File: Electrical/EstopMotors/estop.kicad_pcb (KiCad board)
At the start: 2 copper layers, 20 parts, among them Q1 IRF530NPBF, Q2 IRF530NPBF, Q3 IRF530NPBF, Q4 IRF530NPBF

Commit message: updated to rev 2
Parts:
- removed 10k1, 10k2, 10k3, 10k4, 10k5, 10k6, 10k7, 10k8, 10k9: ROX5SSJ1K8, Resistor_THT:R_Axial_DIN0204_L3.6mm_D1.6mm_P7.62mm_Horizontal
- removed C1: ESK225M050AC3KA, Personal:CAPPRD200W50D500H1250
- removed Control: Conn_01x03, Connector_Wire:SolderWirePad_1x03_P7.62mm_Drill2.5mm
- removed Input 1-4: Conn_01x04, Connector_Wire:SolderWirePad_1x04_P7.62mm_Drill2.5mm
- removed Output 1-4: Conn_01x04, Connector_Wire:SolderWirePad_1x04_P7.62mm_Drill2.5mm
- removed Q1, Q2, Q3, Q4: IRF530NPBF, Personal:TO254P469X1042X1967-3P
- added 10Kr1: ROX5SSJ1K8, Resistor_THT:R_Axial_DIN0204_L3.6mm_D1.6mm_P7.62mm_Horizontal, F.Cu at (78.7, 92.7)
- added 10Kr10: ROX5SSJ1K8, Resistor_THT:R_Axial_DIN0204_L3.6mm_D1.6mm_P7.62mm_Horizontal, F.Cu at (96.5, 73.7)
- added 10Kr11: ROX5SSJ1K8, Resistor_THT:R_Axial_DIN0204_L3.6mm_D1.6mm_P7.62mm_Horizontal, F.Cu at (106.7, 83.8)
- added 10Kr12: ROX5SSJ1K8, Resistor_THT:R_Axial_DIN0204_L3.6mm_D1.6mm_P7.62mm_Horizontal, F.Cu at (101.6, 83.8)
- added 10Kr2: ROX5SSJ1K8, Resistor_THT:R_Axial_DIN0204_L3.6mm_D1.6mm_P7.62mm_Horizontal, F.Cu at (83.8, 92.7)
- added 10Kr3: ROX5SSJ1K8, Resistor_THT:R_Axial_DIN0204_L3.6mm_D1.6mm_P7.62mm_Horizontal, F.Cu at (114.3, 73.7)
- added 10Kr4: ROX5SSJ1K8, Resistor_THT:R_Axial_DIN0204_L3.6mm_D1.6mm_P7.62mm_Horizontal, F.Cu at (99.1, 73.7)
- added 10Kr5: ROX5SSJ1K8, Resistor_THT:R_Axial_DIN0204_L3.6mm_D1.6mm_P7.62mm_Horizontal, F.Cu at (109.2, 83.8)
- added 10Kr6: ROX5SSJ1K8, Resistor_THT:R_Axial_DIN0204_L3.6mm_D1.6mm_P7.62mm_Horizontal, F.Cu at (104.1, 83.8)
- added 10Kr7: ROX5SSJ1K8, Resistor_THT:R_Axial_DIN0204_L3.6mm_D1.6mm_P7.62mm_Horizontal, F.Cu at (81.3, 92.7)
- added 10Kr8: ROX5SSJ1K8, Resistor_THT:R_Axial_DIN0204_L3.6mm_D1.6mm_P7.62mm_Horizontal, F.Cu at (86.4, 92.7)
- added 10Kr9: ROX5SSJ1K8, Resistor_THT:R_Axial_DIN0204_L3.6mm_D1.6mm_P7.62mm_Horizontal, F.Cu at (111.8, 73.7)
- added 1Kr1: ROX5SSJ1K8, Resistor_THT:R_Axial_DIN0204_L3.6mm_D1.6mm_P7.62mm_Horizontal, F.Cu at (73.7, 83.8)
- added 1Kr2: ROX5SSJ1K8, Resistor_THT:R_Axial_DIN0204_L3.6mm_D1.6mm_P7.62mm_Horizontal, F.Cu at (85.1, 83.8)
- added 1Kr3: ROX5SSJ1K8, Resistor_THT:R_Axial_DIN0204_L3.6mm_D1.6mm_P7.62mm_Horizontal, F.Cu at (80.0, 83.8)
- added 1Kr4: ROX5SSJ1K8, Resistor_THT:R_Axial_DIN0204_L3.6mm_D1.6mm_P7.62mm_Horizontal, F.Cu at (91.4, 83.8)
- added Control1: Conn_01x03, Connector_PinHeader_2.54mm:PinHeader_1x03_P2.54mm_Vertical, F.Cu at (96.5, 88.9)
- added Input1: Conn_01x04, Connector_PinHeader_2.54mm:PinHeader_1x04_P2.54mm_Vertical, F.Cu at (78.7, 88.9)
- added M1: IRF530NPBF, Connector_PinHeader_2.54mm:PinHeader_1x03_P2.54mm_Vertical, F.Cu at (73.7, 72.4)
- added M2: IRF530NPBF, Connector_PinHeader_2.54mm:PinHeader_1x03_P2.54mm_Vertical, F.Cu at (85.1, 72.4)
- added M3: IRF530NPBF, Connector_PinHeader_2.54mm:PinHeader_1x03_P2.54mm_Vertical, F.Cu at (80.0, 72.4)
- added M4: IRF530NPBF, Connector_PinHeader_2.54mm:PinHeader_1x03_P2.54mm_Vertical, F.Cu at (91.4, 72.4)
- added MountingHole4: MOUNTINGHOLE, MountingHole:MountingHole_3.2mm_M3, F.Cu at (150.6, 88.8)
- added Output1: Conn_01x04, Connector_PinSocket_2.54mm:PinSocket_1x04_P2.54mm_Vertical, F.Cu at (109.2, 78.7)
- moved MountingHole2 67.0 mm to (165.8, 68.0)
- moved MountingHole3 51.2 mm to (139.7, 73.7)
- moved MountingHole1 30.5 mm to (150.6, 80.8)
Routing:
- net Input2: track 85.6 -> 9.42 mm
- net Input3: track 84.5 -> 9.42 mm
- net Input1: track 83.5 -> 11.0 mm
- net VCC: track 80.5 -> 21.2 mm
- net Input4: track 48.7 -> 11.0 mm
- net Output1: track 27.7 -> 63.6 mm
- net Output2: track 27.7 -> 54.4 mm
- net Output3: track 29.8 -> 44.7 mm
- net Output4: track 27.7 -> 38.1 mm
- net Enable: track 79.8 -> 71.4 mm
- net Net-(1Kr4-Pad2): track 0.00 -> 3.81 mm
- net Net-(1Kr3-Pad2): track 0.00 -> 3.81 mm
- net Net-(1Kr2-Pad2): track 0.00 -> 3.81 mm
- net Net-(1Kr1-Pad2): track 0.00 -> 3.81 mm
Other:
- board text removed: "Gate"

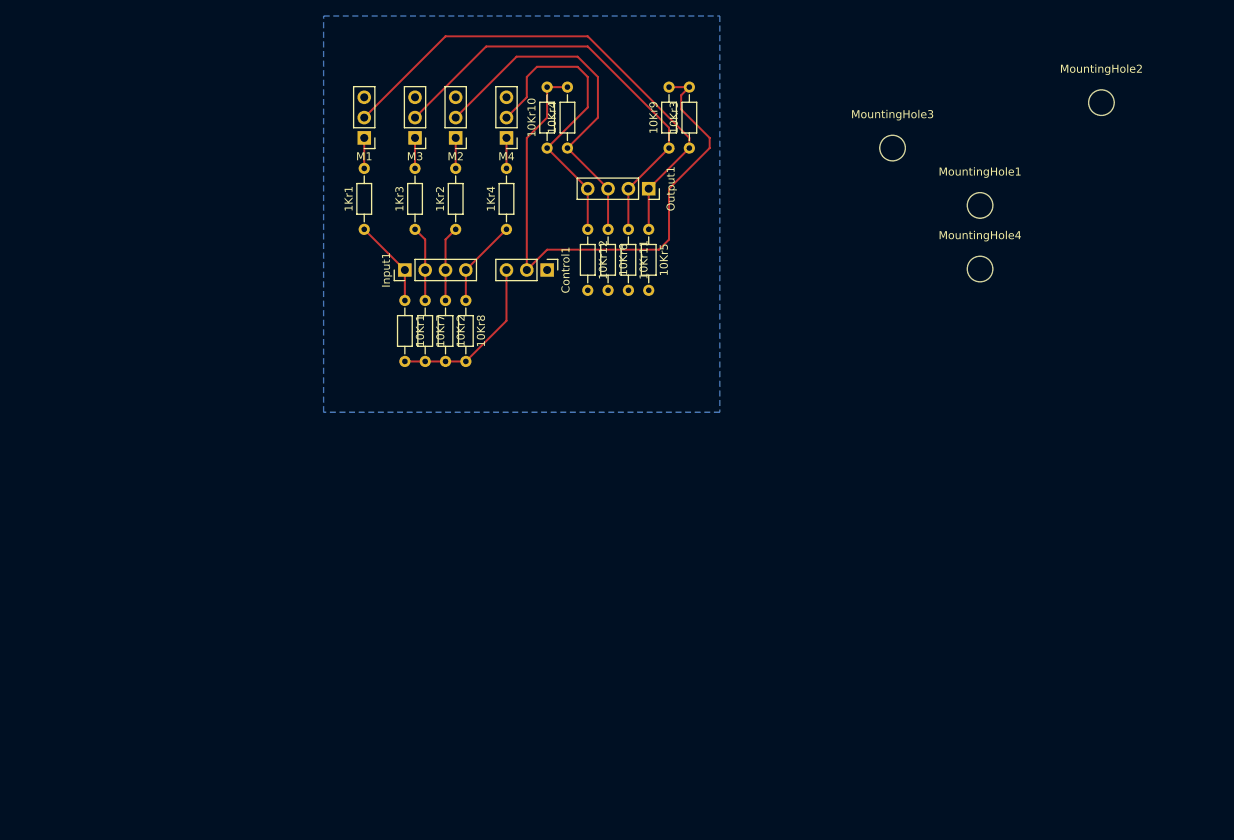
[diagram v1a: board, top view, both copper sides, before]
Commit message: updated pcb and schematic to rev3
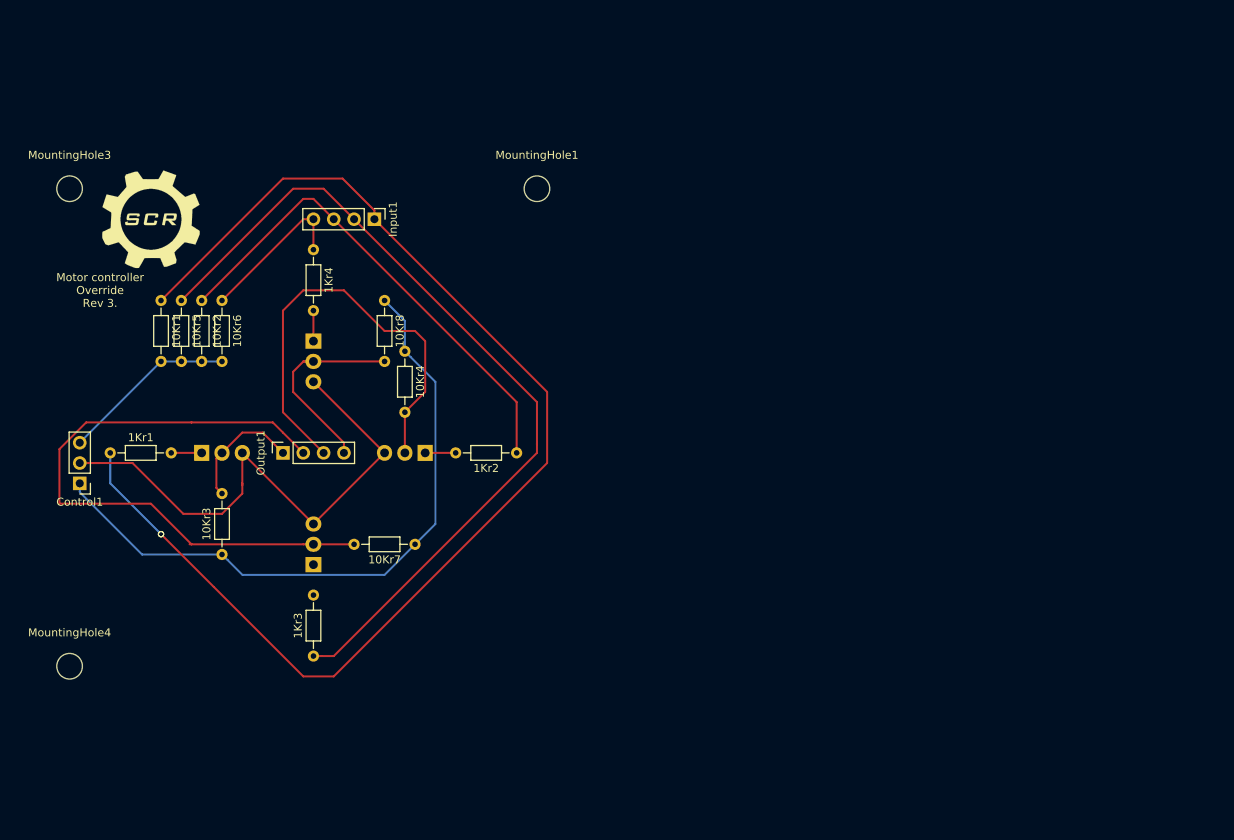
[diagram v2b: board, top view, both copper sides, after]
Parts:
- removed 10Kr10, 10Kr11, 10Kr12, 10Kr9: ROX5SSJ1K8, Resistor_THT:R_Axial_DIN0204_L3.6mm_D1.6mm_P7.62mm_Horizontal
- removed M1, M2, M3, M4: IRF530NPBF, Connector_PinHeader_2.54mm:PinHeader_1x03_P2.54mm_Vertical
- removed MountingHole2: MOUNTINGHOLE, MountingHole:MountingHole_3.2mm_M3
- added .: ., SCR:scr-logo, F.Cu at (47.0, 82.5)
- added Q1: IRF9530N, Package_TO_SOT_THT:TO-220-3_Vertical, B.Cu at (53.3, 111.8)
- added Q2: IRF9530N, Package_TO_SOT_THT:TO-220-3_Vertical, B.Cu at (81.3, 111.8)
- added Q3: IRF9530N, Package_TO_SOT_THT:TO-220-3_Vertical, B.Cu at (67.3, 125.7)
- added Q4: IRF9530N, Package_TO_SOT_THT:TO-220-3_Vertical, B.Cu at (67.3, 97.8)
- moved MountingHole4 124.2 mm to (36.8, 138.4)
- moved MountingHole3 103.0 mm to (36.8, 78.7)
- moved 10Kr3 77.4 mm to (55.9, 124.5)
- moved Control1 64.2 mm to (38.1, 115.6), turned to 180 degrees
- moved 10Kr5 59.1 mm to (50.8, 92.7)
- moved Output1 56.4 mm to (63.5, 111.8), turned to 90 degrees
- moved MountingHole1 55.4 mm to (95.2, 78.7)
- moved 1Kr3 54.8 mm to (67.3, 137.2)
- moved 10Kr6 49.1 mm to (55.9, 92.7)
- moved 1Kr1 42.3 mm to (41.9, 111.8), turned to 0 degrees
- moved 10Kr4 32.5 mm to (78.7, 99.1), turned to 270 degrees
- moved 10Kr7 30.5 mm to (80.0, 123.2), turned to 180 degrees
- moved 10Kr1 30.5 mm to (48.3, 92.7)
- moved 10Kr2 30.5 mm to (53.3, 92.7)
- moved 1Kr2 29.0 mm to (92.7, 111.8), turned to 180 degrees
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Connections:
- 10Kr3 pad 1: Output1 -> GND
- 10Kr3 pad 2: Enable -> Output1
- 10Kr4 pad 1: Output3 -> GND
- 10Kr4 pad 2: Enable -> Output3
- 10Kr5 pad 1: Output1 -> Input2
- 10Kr5 pad 2: GND -> VCC
- 10Kr6 pad 1: Output3 -> Input4
- 10Kr6 pad 2: GND -> VCC
- 10Kr7 pad 1: Input2 -> GND
- 10Kr7 pad 2: VCC -> Output2
- 10Kr8 pad 1: Input4 -> GND
- 10Kr8 pad 2: VCC -> Output4
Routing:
- net Input1: track 11.0 -> 154.6 mm, vias 0 -> 2
- net Input2: track 9.42 -> 106.3 mm
- net GND: track 0.00 -> 83.0 mm
- net Input3: track 9.42 -> 61.5 mm
- net Output1: track 63.6 -> 15.4 mm
- net Output2: track 54.4 -> 79.5 mm
- net Output4: track 38.1 -> 26.0 mm
- net Output3: track 44.7 -> 56.4 mm
- net Input4: track 11.0 -> 19.4 mm
- net Net-(1Kr3-Pad2): track 3.81 -> 0.00 mm
- net Enable: track 71.4 -> 69.6 mm
- net VCC: track 21.2 -> 22.0 mm
- removed copper zone on B.Cu, net GND
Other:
- board text added: "Motor controller Override Rev 3."

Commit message: updated to rev 3 and added correct designators. Uploaded rev 3 schematic
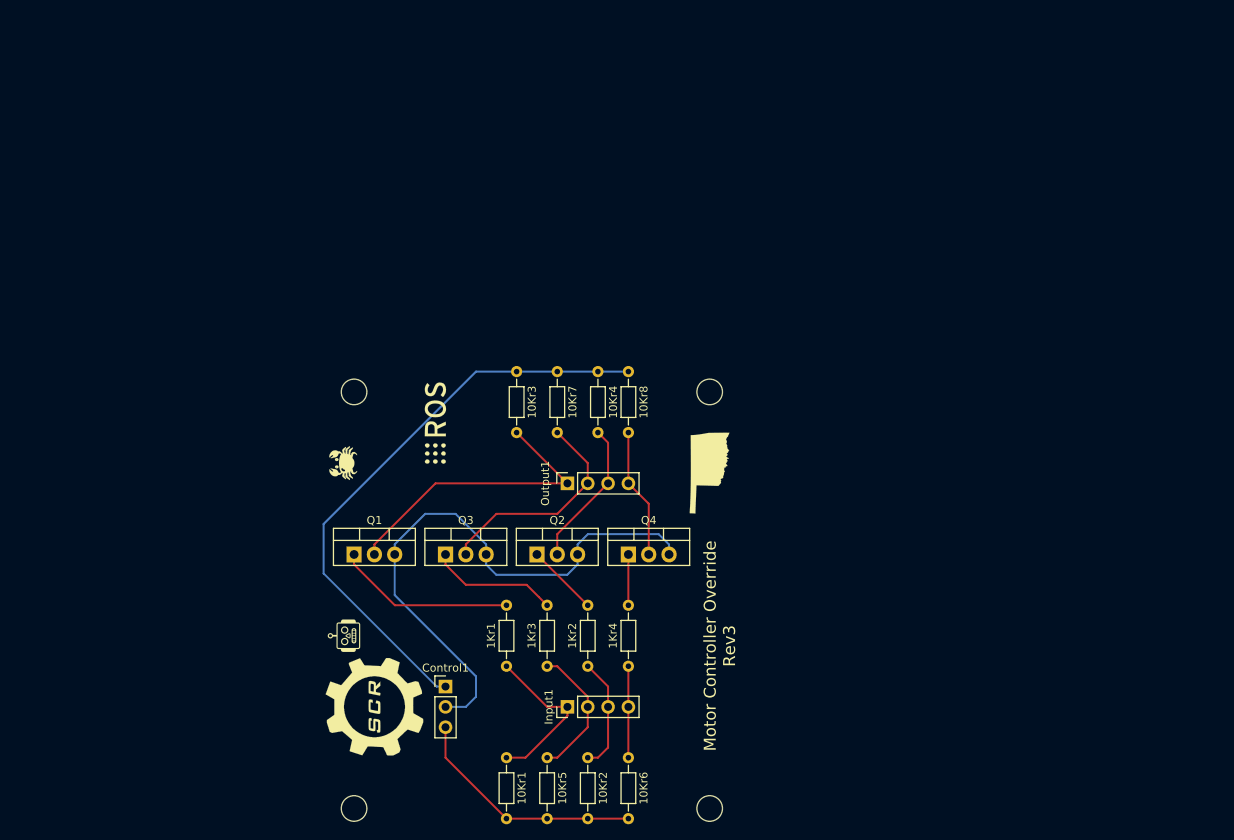
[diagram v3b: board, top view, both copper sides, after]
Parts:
- removed .: ., SCR:scr-logo
- added G***: LOGO, SCR:ROS, F.Cu at (82.5, 108.0)
- added G***: LOGO, SCR:robot-image, F.Cu at (71.1, 134.6)
- added G***: LOGO, SCR:oklahoma-image, F.Cu at (116.8, 114.3)
- added G***: LOGO, SCR:crab-image, F.Cu at (71.1, 113.0)
- added G***: LOGO, SCR:scr-logo, F.Cu at (74.9, 143.5)
- added MountingHole2: MOUNTINGHOLE, MountingHole:MountingHole_3.2mm_M3, F.Cu at (116.8, 104.1)
- Q1, Q2, Q3, Q4: moved to F.Cu
- moved MountingHole3 85.2 mm to (72.4, 156.2)
- moved MountingHole4 82.0 mm to (116.8, 156.2)
- moved 10Kr6 76.5 mm to (106.7, 149.9)
- moved 10Kr2 74.8 mm to (101.6, 149.9)
- moved 10Kr5 73.2 mm to (96.5, 149.9)
- moved 10Kr1 71.6 mm to (91.4, 149.9)
- moved Input1 65.6 mm to (99.1, 143.5), turned to 90 degrees
- moved 1Kr4 65.3 mm to (106.7, 138.4), turned to 90 degrees
- moved 1Kr1 56.3 mm to (91.4, 138.4), turned to 90 degrees
- moved Control1 52.3 mm to (83.8, 141.0), turned to 0 degrees
- moved Q4 47.6 mm to (106.7, 124.5), turned to 0 degrees
- moved 10Kr3 43.3 mm to (92.7, 101.6), turned to 270 degrees
- moved Output1 35.8 mm to (99.1, 115.6)
- moved MountingHole1 34.2 mm to (72.4, 104.1)
- moved 10Kr8 31.8 mm to (106.7, 101.6)
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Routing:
- net Input1: track 154.6 -> 20.6 mm, vias 2 -> 0
- net Input2: track 106.3 -> 17.1 mm
- net Output2: track 79.5 -> 27.6 mm
- net Input3: track 61.5 -> 14.3 mm
- net Output3: track 56.4 -> 18.4 mm
- net Output1: track 15.4 -> 37.5 mm
- net Net-(1Kr1-Pad2): track 3.81 -> 22.4 mm
- net Net-(1Kr3-Pad2): track 0.00 -> 16.1 mm
- net GND: track 83.0 -> 73.3 mm
- net Output4: track 26.0 -> 16.3 mm
- net Input4: track 19.4 -> 11.4 mm
- net VCC: track 22.0 -> 29.8 mm
- net Net-(1Kr2-Pad2): track 3.81 -> 8.98 mm
- net Enable: track 69.6 -> 73.4 mm
- net Net-(1Kr4-Pad2): track 3.81 -> 6.35 mm
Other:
- board text added: "Motor Controller Override Rev3"
- board text removed: "Motor controller Override Rev 3."
